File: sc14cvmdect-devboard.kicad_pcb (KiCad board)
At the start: 4 copper layers, 80 x 90 mm, 95 parts, among them J1 Conn_01x08, J2 USB_C_Receptacle_USB2.0_16P, J3 Conn_01x03, J4 Conn_01x18, J6 Conn_01x18, SW1 SW_Push, U1 TLV1117LV33, U2 SC14CVMDECT, U3 FT230XQ

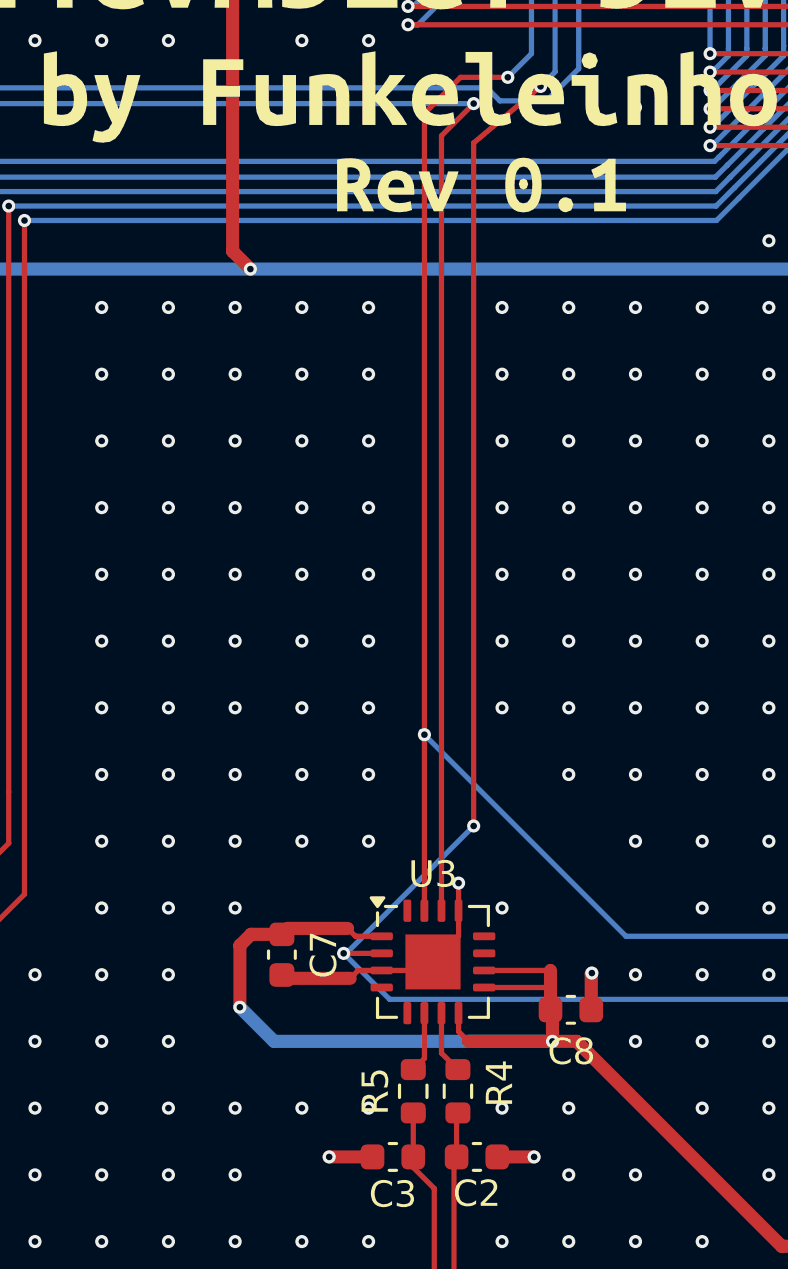
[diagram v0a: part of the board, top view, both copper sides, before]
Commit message: Add 1V8 voltage regulator to fix internal UART voltage.
This commits adds a voltage regulator to change the voltage at the
VCCIO pin of the internal UART converter to 1V8.
This design was not tested in production/hardware yet but instead
is a hot fix to offer an alternative to the manufacturing of boards
with the wrong UART voltage.
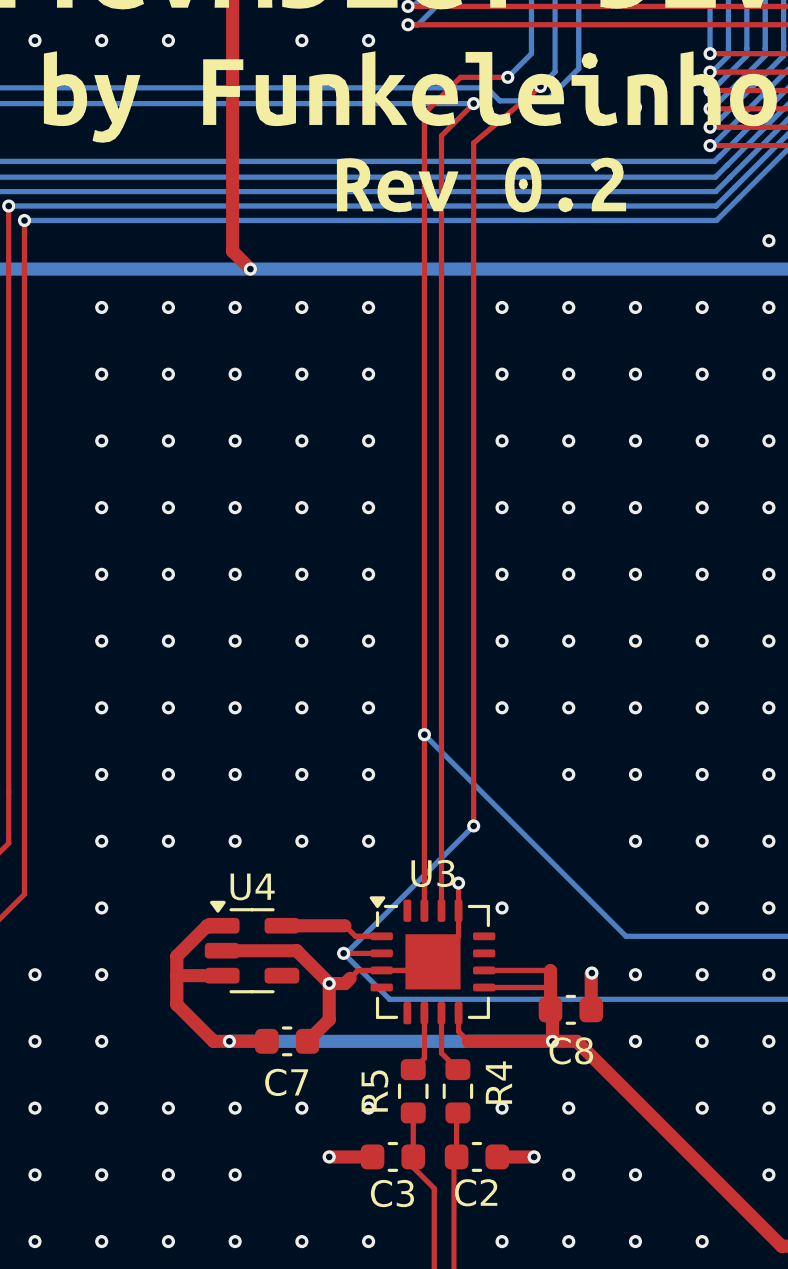
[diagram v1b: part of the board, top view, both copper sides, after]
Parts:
- removed kibuzzard-67577969: G***, kibuzzard-67577969
- added U4: MIC5317-1.8xM5, Package_TO_SOT_SMD:SOT-23-5, F.Cu at (143.1, 105.8)
- added kibuzzard-676BF11C: G***, kibuzzard-676BF11C, F.Cu at (151.8, 76.6)
- moved C7 3.31 mm to (144.4, 109.2), turned to 0 degrees
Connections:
- U3 pad 1: +3V3 -> Net-(U3-VCCIO)
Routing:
- net GND: track 116.9 -> 122.2 mm, vias 397 -> 394
- net Net-(U3-VCCIO): track 0.00 -> 3.97 mm
- net +3V3: track 244.9 -> 246.4 mm
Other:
- board text added: "This 1V8 voltage regulator should fix the design issue from Rev0.1 but was not tested in hardware so far."
- board text removed: "Pin 1 of U3 is wrongly connected to 3V3 in this revision. Connect to 1V8 if you want to receive data with the internal UART."

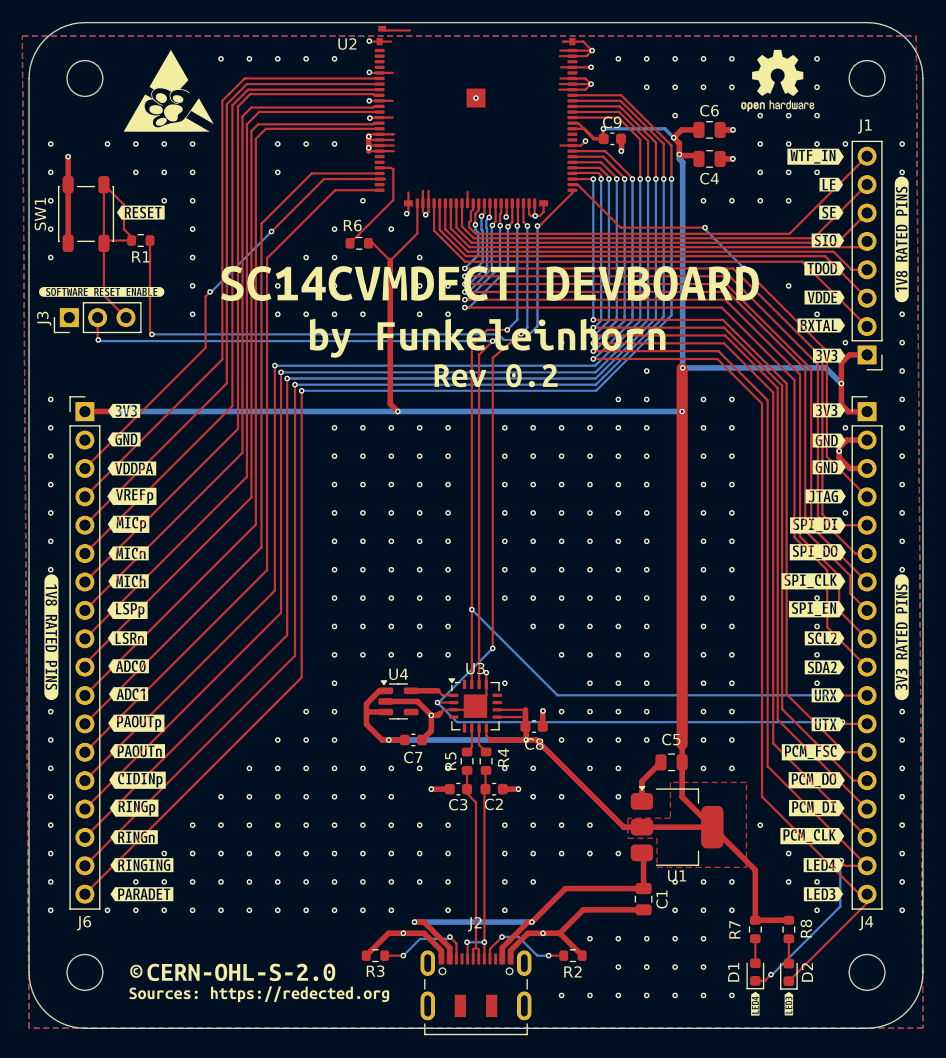
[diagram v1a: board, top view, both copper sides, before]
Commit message: tweaks
Added
 - +1V8 on left pinheader
 - VBUS on left pinheader

Moved RESET Button up a little
Moved Jumper up a little
Moved right pinheaders by 1.27mm so they match a standard raster
breadboard
Replaced fancy pin labels with readable labels
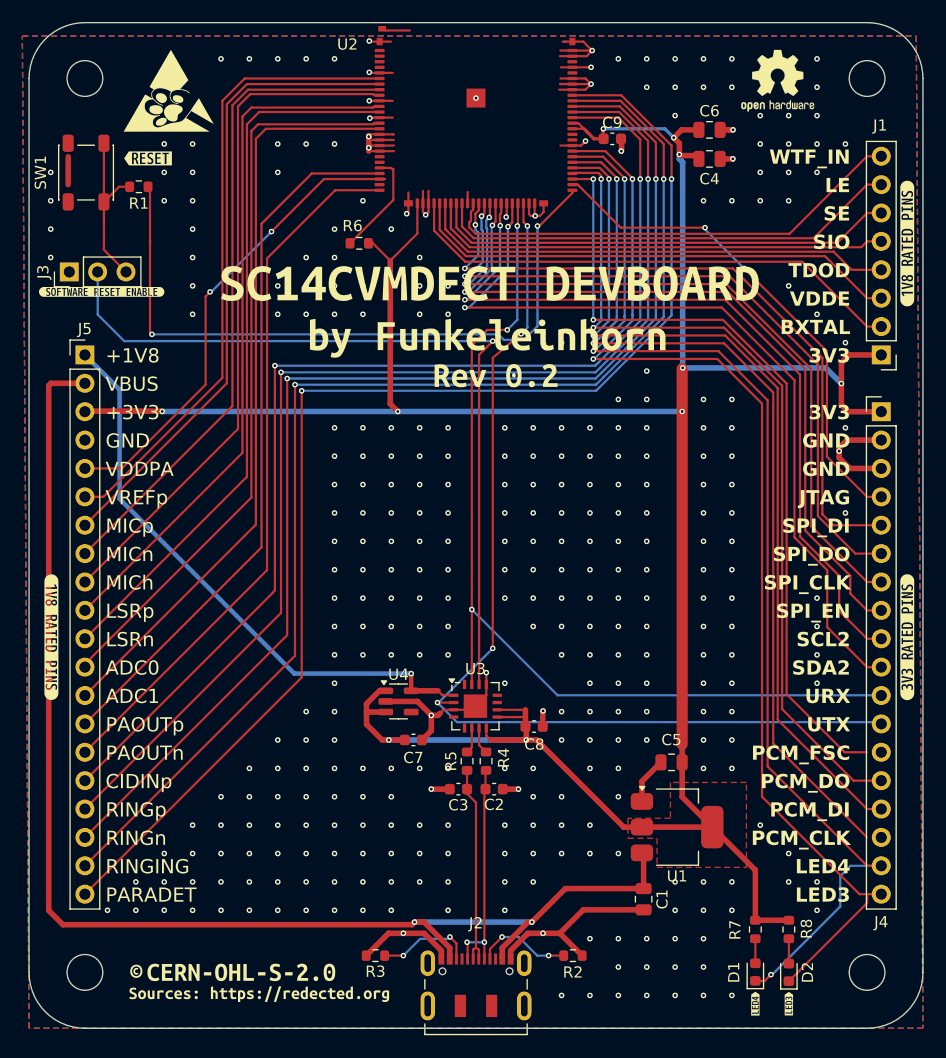
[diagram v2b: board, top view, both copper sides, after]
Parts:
- removed J6: Conn_01x18, Connector_PinHeader_2.54mm:PinHeader_1x18_P2.54mm_Vertical
- removed kibuzzard-67575DD6: G***, kibuzzard-67575DD6
- removed kibuzzard-67575DF0: G***, kibuzzard-67575DF0
- removed kibuzzard-67575E60: G***, kibuzzard-67575E60
- removed kibuzzard-67576033: G***, kibuzzard-67576033
- removed kibuzzard-6757604E: G***, kibuzzard-6757604E
- removed kibuzzard-67576075: G***, kibuzzard-67576075
- removed kibuzzard-6757607D: G***, kibuzzard-6757607D
- removed kibuzzard-675760A1: G***, kibuzzard-675760A1
- removed kibuzzard-675760B0: G***, kibuzzard-675760B0
- removed kibuzzard-67576138: G***, kibuzzard-67576138
- removed kibuzzard-67576147: G***, kibuzzard-67576147
- removed kibuzzard-6757616E: G***, kibuzzard-6757616E
- removed kibuzzard-67576184: G***, kibuzzard-67576184
- removed kibuzzard-675761BC: G***, kibuzzard-675761BC
- removed kibuzzard-675761D3: G***, kibuzzard-675761D3
- removed kibuzzard-675761E9: G***, kibuzzard-675761E9
- removed kibuzzard-6757620D: G***, kibuzzard-6757620D
- removed kibuzzard-6757621E: G***, kibuzzard-6757621E
- removed kibuzzard-6757634F: G***, kibuzzard-6757634F
- removed kibuzzard-6757635E: G***, kibuzzard-6757635E
- removed kibuzzard-6757636C: G***, kibuzzard-6757636C
- removed kibuzzard-6757638A: G***, kibuzzard-6757638A
- removed kibuzzard-6757639A: G***, kibuzzard-6757639A
- removed kibuzzard-675763C9: G***, kibuzzard-675763C9
- removed kibuzzard-675763D6: G***, kibuzzard-675763D6
- removed kibuzzard-675763F4: G***, kibuzzard-675763F4
- removed kibuzzard-67576478: G***, kibuzzard-67576478
- removed kibuzzard-67576487: G***, kibuzzard-67576487
- removed kibuzzard-67576490: G***, kibuzzard-67576490
- removed kibuzzard-675764D8: G***, kibuzzard-675764D8
- removed kibuzzard-6757652F: G***, kibuzzard-6757652F
- removed kibuzzard-67576547: G***, kibuzzard-67576547
- removed kibuzzard-67576569: G***, kibuzzard-67576569
- removed kibuzzard-6757657B: G***, kibuzzard-6757657B
- removed kibuzzard-6757659F: G***, kibuzzard-6757659F
- removed kibuzzard-675765AC: G***, kibuzzard-675765AC
- removed kibuzzard-675765C1: G***, kibuzzard-675765C1
- removed kibuzzard-675765D1: G***, kibuzzard-675765D1
- removed kibuzzard-6757660D: G***, kibuzzard-6757660D
- removed kibuzzard-6757661A: G***, kibuzzard-6757661A
- removed kibuzzard-67576627: G***, kibuzzard-67576627
- removed kibuzzard-6757663B: G***, kibuzzard-6757663B
- removed kibuzzard-67576652: G***, kibuzzard-67576652
- removed kibuzzard-67576660: G***, kibuzzard-67576660
- added J5: Conn_01x20, Connector_PinHeader_2.54mm:PinHeader_1x20_P2.54mm_Vertical, F.Cu at (115.0, 74.7)
- moved kibuzzard-67575DB5 4.89 mm to (120.7, 57.1)
- moved R1 4.81 mm to (119.8, 59.7)
- moved J3 4.09 mm to (113.6, 67.3)
- moved SW1 3.70 mm to (115.1, 58.4)
- moved J1 1.27 mm to (186.3, 74.7)
- moved J4 1.27 mm to (186.3, 79.8)
- moved kibuzzard-67575F62 0.62 mm to (188.6, 64.8)
- moved kibuzzard-67575F78 0.50 mm to (188.6, 100.0)
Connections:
- net Net-(U3-VCCIO) renamed 1V8
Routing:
- net VBUS: track 34.7 -> 118.4 mm
- net 1V8: track 3.97 -> 52.3 mm, vias 0 -> 1
- net Net-(J3-Pin_3): track 21.4 -> 15.2 mm
- net Net-(U2-RSTn): track 57.3 -> 62.4 mm
- net Net-(J3-Pin_2): track 68.6 -> 71.4 mm, vias 2 -> 1
- net GND: track 122.2 -> 119.5 mm, vias 394 -> 354
- net +3V3: track 246.4 -> 249.0 mm
- net Net-(J5-Pin_5): track 40.8 -> 42.7 mm
- net Net-(D1-K): track 102.0 -> 103.3 mm, vias 4 -> 3
- net Net-(J4-Pin_8): track 66.5 -> 67.7 mm
- net Net-(J4-Pin_9): track 69.1 -> 70.4 mm
- net Net-(J4-Pin_6): track 61.8 -> 63.1 mm
- net Net-(J4-Pin_5): track 60.3 -> 61.5 mm
- net Net-(J4-Pin_4): track 43.6 -> 44.8 mm
- net Net-(J4-Pin_15): track 77.9 -> 79.1 mm
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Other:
- board text added: "+1V8"
- board text added: "+3V3"
- board text added: "3V3"
- board text added: "ADC0"
- board text added: "ADC1"
- board text added: "BXTAL"
- board text added: "CIDINp"
- board text added: "GND"
- board text added: "JTAG"
- board text added: "LE"
- board text added: "LED3"
- board text added: "LED4"
- board text added: "LSRn"
- board text added: "LSRp"
- board text added: "MICh"
- board text added: "MICn"
- board text added: "MICp"
- board text added: "PAOUTn"
- board text added: "PAOUTp"
- board text added: "PARADET"
- board text added: "PCM_CLK"
- board text added: "PCM_DI"
- board text added: "PCM_DO"
- board text added: "PCM_FSC"
- board text added: "RINGING"
- board text added: "RINGn"
- board text added: "RINGp"
- board text added: "SCL2"
- board text added: "SDA2"
- board text added: "SE"
- board text added: "SIO"
- board text added: "SPI_CLK"
- board text added: "SPI_DI"
- board text added: "SPI_DO"
- board text added: "SPI_EN"
- board text added: "TDOD"
- board text added: "URX"
- board text added: "UTX"
- board text added: "VBUS"
- board text added: "VDDE"
- board text added: "VDDPA"
- board text added: "VREFp"
- board text added: "WTF_IN"
